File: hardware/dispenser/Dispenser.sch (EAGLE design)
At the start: 64 parts, among them J1 AVR_Prog, J2 RJ45-8PTH, Q1 NFET-SO8, Q2 NFET, Q3 NFET, Q4 NFET, Q5 MOSFET-NCHANNELSMD, U1 ATMEGA168, U10 HALL-EFFECT, U2 OPAMP-DUAL, U3 OPTO-TLP185, U4 MPX10DP, U5 VREG-5V-LDO-AP1117SOT89-3L, U6 WS2801, U7 HALL-EFFECT, U8 HALL-EFFECT, U9 HALL-EFFECT

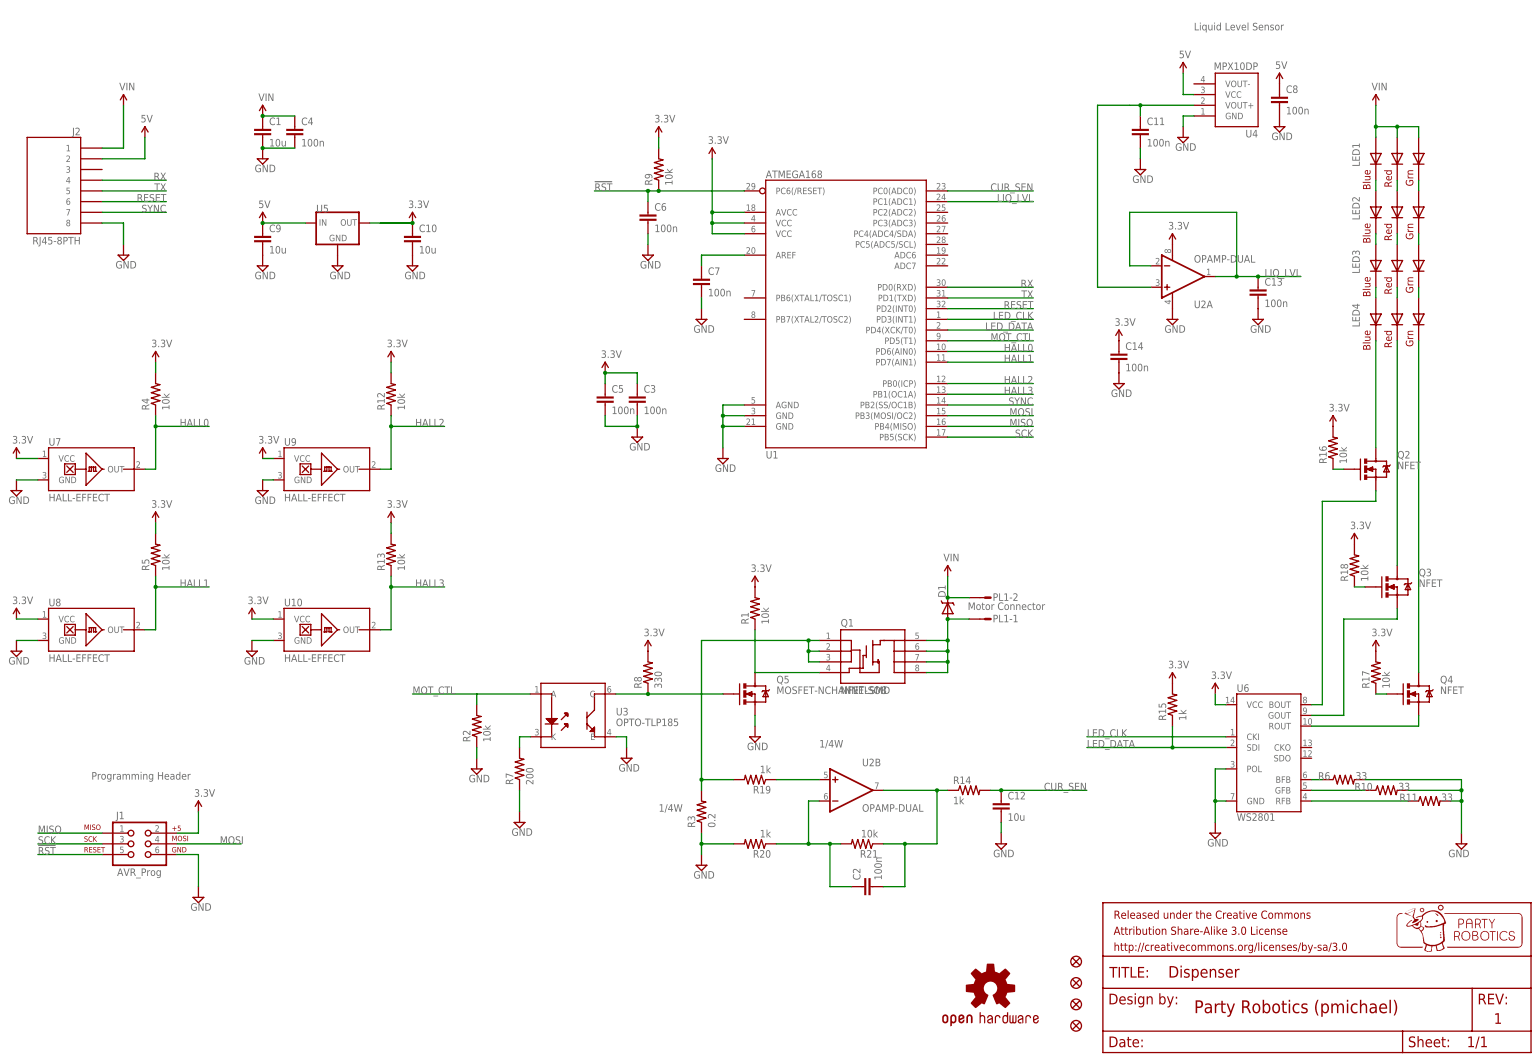
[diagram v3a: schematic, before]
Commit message: Current sense cap to 100u, and opto inputs changed again
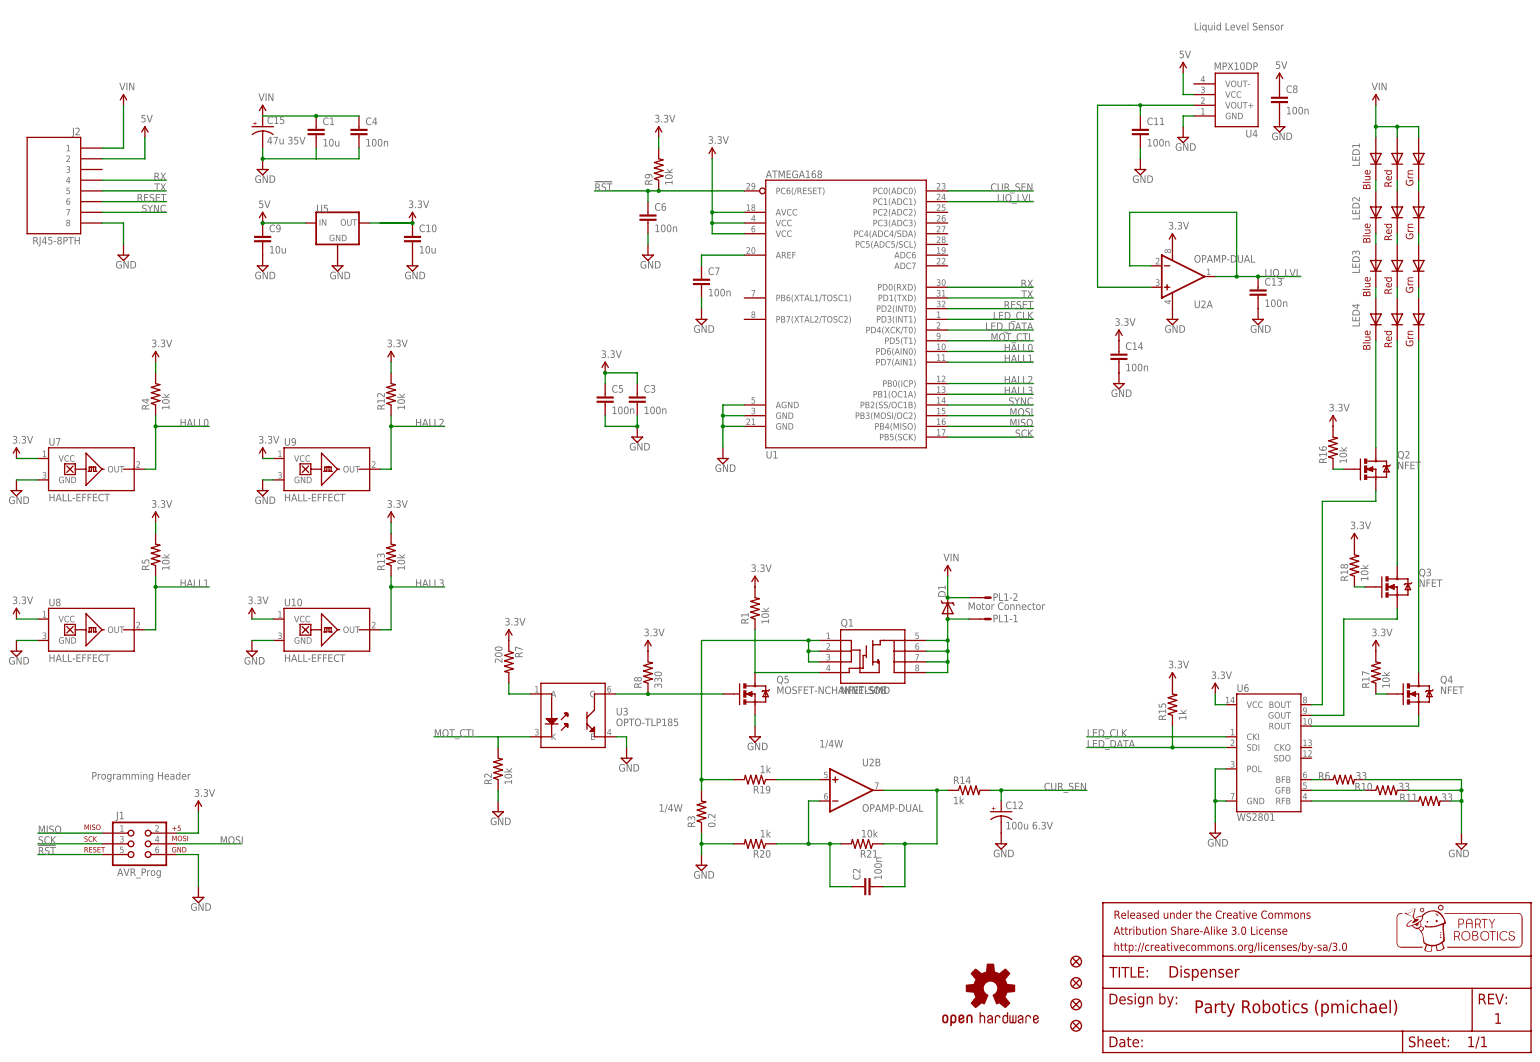
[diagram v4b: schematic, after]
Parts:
- added C15: 47u 35V, SparkFun-Capacitors:CAP_POLD
- C12: value 10u -> 100u 6.3V; device SparkFun-Capacitors:CAP1206 -> SparkFun-Capacitors:CAP_POLD
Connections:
- new net N$16: R7.2, U3.A
- net 3.3V: now also R7.1
- net CUR_SEN: now also C12.+; no longer C12.1
- net GND: now also C12.-; no longer C12.2, R7.1
- net MOT_CTL: now also U3.K; no longer U3.A
- net N$15: now also C15.-; no longer R7.2, U3.K
- net VIN: now also C15.+
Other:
- moved on the sheet: C1, C4, R2, R7
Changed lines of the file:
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@@
 <part name="R2" library="SparkFun-Resistors" deviceset="RESISTOR" device="0603-RES" value="10k"/>
 <part name="SUPPLY4" library="supply2" deviceset="GND" device=""/>
-<part name="C12" library="SparkFun-Capacitors" deviceset="CAP" device="1206" value="10u"/>
 <part name="SUPPLY5" library="supply2" deviceset="GND" device=""/>
 <part name="R14" library="SparkFun-Resistors" deviceset="RESISTOR" device="0603-RES" value="1k"/>
@@
 <part name="P+18" library="SparkFun-Aesthetics" deviceset="3.3V" device=""/>
 <part name="D1" library="pierre" deviceset="B330A" device=""/>
-<part name="SUPPLY22" library="supply2" deviceset="GND" device=""/>
+<part name="P+10" library="SparkFun-Aesthetics" deviceset="3.3V" device=""/>
+<part name="C12" library="SparkFun-Capacitors" deviceset="CAP_POL" device="D" value="100u 6.3V"/>
+<part name="C15" library="SparkFun-Capacitors" deviceset="CAP_POL" device="D" value="47u 35V"/>
 </parts>
 <sheets>
@@
 <instance part="C3" gate="G$1" x="172.72" y="157.48"/>
 <instance part="SUPPLY2" gate="GND" x="193.04" y="144.78"/>
-<instance part="C1" gate="G$1" x="83.82" y="220.98"/>
-<instance part="SUPPLY6" gate="GND" x="83.82" y="215.9"/>
+<instance part="C1" gate="G$1" x="96.52" y="220.98"/>
+<instance part="SUPPLY6" gate="GND" x="83.82" y="213.36"/>
 <instance part="U$13" gate="G$1" x="83.82" y="226.06"/>
 <instance part="Q1" gate="G$1" x="228.6" y="99.06"/>
 <instance part="U$14" gate="G$1" x="246.38" y="116.84"/>
 <instance part="U3" gate="G$1" x="157.48" y="83.82"/>
-<instance part="R7" gate="G$1" x="144.78" y="71.12" rot="R90"/>
+<instance part="R7" gate="G$1" x="142.24" y="96.52" rot="R270"/>
 <instance part="SUPPLY7" gate="GND" x="170.18" y="73.66"/>
 <instance part="R8" gate="G$1" x="175.26" y="93.98" rot="R90"/>
@@
 <instance part="GND" gate="GND" x="299.72" y="177.8"/>
 <instance part="U$3" gate="G$1" x="347.98" y="228.6"/>
-<instance part="C4" gate="G$1" x="91.44" y="220.98"/>
+<instance part="C4" gate="G$1" x="106.68" y="220.98"/>
 <instance part="R6" gate="G$1" x="340.36" y="68.58" smashed="yes">
 <attribute name="NAME" x="334.264" y="68.5546" size="1.778" layer="95"/>
@@
 <attribute name="VALUE" x="363.474" y="63.5" size="1.778" layer="96"/>
 </instance>
-<instance part="R2" gate="G$1" x="134.62" y="81.28" rot="R90"/>
-<instance part="SUPPLY4" gate="GND" x="134.62" y="71.12"/>
-<instance part="C12" gate="G$1" x="259.08" y="60.96"/>
+<instance part="R2" gate="G$1" x="139.7" y="71.12" rot="R90"/>
+<instance part="SUPPLY4" gate="GND" x="139.7" y="60.96"/>
 <instance part="SUPPLY5" gate="GND" x="259.08" y="53.34"/>
 <instance part="R14" gate="G$1" x="251.46" y="66.04"/>
@@
 <instance part="P+18" gate="G$1" x="200.66" y="114.3"/>
 <instance part="D1" gate="G$1" x="246.38" y="109.22" rot="R90"/>
-<instance part="SUPPLY22" gate="GND" x="144.78" y="58.42"/>
+<instance part="P+10" gate="G$1" x="142.24" y="101.6"/>
+<instance part="C12" gate="G$1" x="259.08" y="60.96"/>
+<instance part="C15" gate="G$1" x="83.82" y="223.52"/>
 </instances>
 <busses>
@@
 <pinref part="SUPPLY6" gate="GND" pin="GND"/>
 <pinref part="C4" gate="G$1" pin="2"/>
-<wire x1="91.44" y1="218.44" x2="83.82" y2="218.44" width="0.1524" layer="91"/>
-<junction x="83.82" y="218.44"/>
+<wire x1="106.68" y1="218.44" x2="106.68" y2="215.9" width="0.1524" layer="91"/>
+<wire x1="106.68" y1="215.9" x2="96.52" y2="215.9" width="0.1524" layer="91"/>
+<junction x="83.82" y="215.9"/>
+<wire x1="83.82" y1="215.9" x2="96.52" y2="215.9" width="0.1524" layer="91"/>
+<wire x1="96.52" y1="215.9" x2="96.52" y2="218.44" width="0.1524" layer="91"/>
 </segment>
 <segment>
@@
 <pinref part="R2" gate="G$1" pin="1"/>
 <pinref part="SUPPLY4" gate="GND" pin="GND"/>
-<wire x1="134.62" y1="76.2" x2="134.62" y2="73.66" width="0.1524" layer="91"/>
+<wire x1="139.7" y1="66.04" x2="139.7" y2="63.5" width="0.1524" layer="91"/>
 </segment>
 <segment>
-<pinref part="C12" gate="G$1" pin="2"/>
 <pinref part="SUPPLY5" gate="GND" pin="GND"/>
-<wire x1="259.08" y1="58.42" x2="259.08" y2="55.88" width="0.1524" layer="91"/>
+<pinref part="C12" gate="G$1" pin="-"/>
 </segment>
 <segment>
@@
 <wire x1="200.66" y1="81.28" x2="200.66" y2="83.82" width="0.1524" layer="91"/>
 </segment>
-<segment>
-<pinref part="R7" gate="G$1" pin="1"/>
-<wire x1="144.78" y1="66.04" x2="144.78" y2="60.96" width="0.1524" layer="91"/>
-<pinref part="SUPPLY22" gate="GND" pin="GND"/>
-</segment>
 </net>
 <net name="5V" class="0">
@@
 <pinref part="P+18" gate="G$1" pin="3.3V"/>
 </segment>
+<segment>
+<pinref part="R7" gate="G$1" pin="1"/>
+<pinref part="P+10" gate="G$1" pin="3.3V"/>
+</segment>
 </net>
 <net name="LED_CLK" class="0">
@@
 </segment>
 <segment>
-<pinref part="C12" gate="G$1" pin="1"/>
-<wire x1="259.08" y1="66.04" x2="279.4" y2="66.04" width="0.1524" layer="91"/>
-<junction x="259.08" y="66.04"/>
 <wire x1="256.54" y1="66.04" x2="259.08" y2="66.04" width="0.1524" layer="91"/>
 <label x="279.4" y="66.04" size="1.778" layer="95" rot="MR0"/>
 <pinref part="R14" gate="G$1" pin="2"/>
+<pinref part="C12" gate="G$1" pin="+"/>
+<wire x1="259.08" y1="63.5" x2="259.08" y2="66.04" width="0.1524" layer="91"/>
+<wire x1="259.08" y1="66.04" x2="279.4" y2="66.04" width="0.1524" layer="91"/>
+<junction x="259.08" y="66.04"/>
 </segment>
 </net>
@@
 <pinref part="U$13" gate="G$1" pin="VIN"/>
 <pinref part="C4" gate="G$1" pin="1"/>
-<wire x1="91.44" y1="226.06" x2="83.82" y2="226.06" width="0.1524" layer="91"/>
-<junction x="83.82" y="226.06"/>
+<wire x1="106.68" y1="226.06" x2="96.52" y2="226.06" width="0.1524" layer="91"/>
+<junction x="96.52" y="226.06"/>
+<pinref part="C15" gate="G$1" pin="+"/>
+<wire x1="96.52" y1="226.06" x2="83.82" y2="226.06" width="0.1524" layer="91"/>
 </segment>
 <segment>
@@
 <net name="MOT_CTL" class="0">
 <segment>
-<label x="119.38" y="88.9" size="1.778" layer="95"/>
-<wire x1="134.62" y1="86.36" x2="134.62" y2="88.9" width="0.2032" layer="91"/>
-<wire x1="134.62" y1="88.9" x2="119.38" y2="88.9" width="0.2032" layer="91"/>
+<label x="124.46" y="78.74" size="1.778" layer="95"/>
+<wire x1="139.7" y1="76.2" x2="139.7" y2="78.74" width="0.2032" layer="91"/>
+<wire x1="139.7" y1="78.74" x2="124.46" y2="78.74" width="0.2032" layer="91"/>
 <pinref part="R2" gate="G$1" pin="2"/>
-<pinref part="U3" gate="G$1" pin="A"/>
-<wire x1="134.62" y1="88.9" x2="147.32" y2="88.9" width="0.1524" layer="91"/>
+<pinref part="U3" gate="G$1" pin="K"/>
+<wire x1="147.32" y1="78.74" x2="139.7" y2="78.74" width="0.1524" layer="91"/>
 </segment>
 <segment>
@@
 </segment>
 </net>
-<net name="N$15" class="0">
+<net name="N$16" class="0">
 <segment>
 <pinref part="R7" gate="G$1" pin="2"/>
-<wire x1="144.78" y1="76.2" x2="144.78" y2="78.74" width="0.1524" layer="91"/>
-<pinref part="U3" gate="G$1" pin="K"/>
-<wire x1="144.78" y1="78.74" x2="147.32" y2="78.74" width="0.1524" layer="91"/>
+<wire x1="142.24" y1="91.44" x2="142.24" y2="88.9" width="0.1524" layer="91"/>
+<pinref part="U3" gate="G$1" pin="A"/>
+<wire x1="142.24" y1="88.9" x2="147.32" y2="88.9" width="0.1524" layer="91"/>
+</segment>
+</net>
+<net name="N$15" class="0">
+<segment>
+<pinref part="C15" gate="G$1" pin="-"/>
+<wire x1="83.82" y1="218.44" x2="83.82" y2="215.9" width="0.1524" layer="91"/>
 </segment>
 </net>

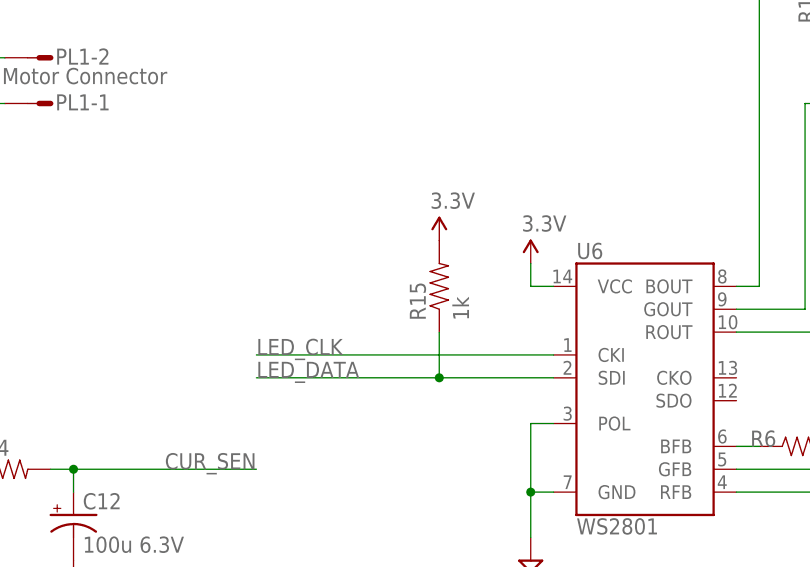
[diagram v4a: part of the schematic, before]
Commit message: removed LED_DATA pull up
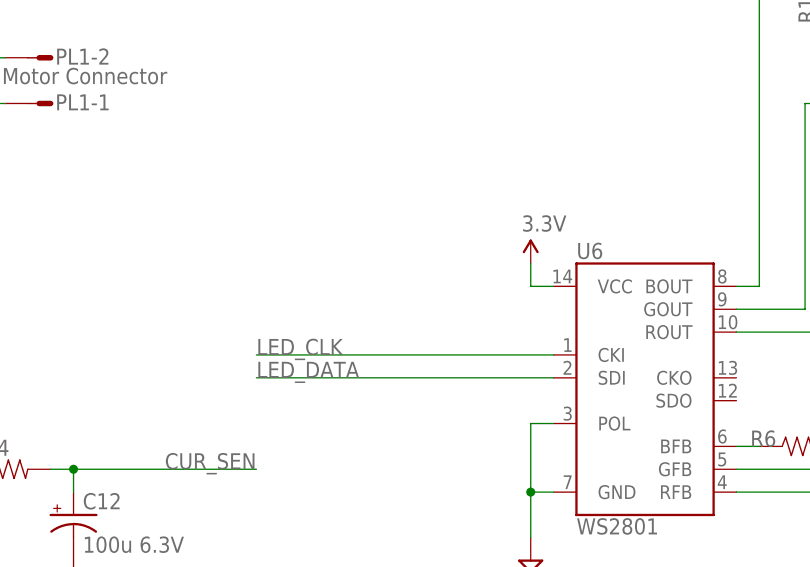
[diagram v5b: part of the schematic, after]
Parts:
- removed R15: 1k, SparkFun-Resistors:RESISTOR0603-RES
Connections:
- net 3.3V: no longer R15.2
- net LED_DATA: no longer R15.1
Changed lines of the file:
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@@
 <part name="SUPPLY23" library="supply2" deviceset="GND" device=""/>
 <part name="SUPPLY24" library="supply2" deviceset="GND" device=""/>
-<part name="R15" library="SparkFun-Resistors" deviceset="RESISTOR" device="0603-RES" value="1k"/>
-<part name="P+21" library="SparkFun-Aesthetics" deviceset="3.3V" device=""/>
 <part name="C11" library="SparkFun" deviceset="CAP" device="0603-CAP" value="100n"/>
 <part name="SUPPLY25" library="supply2" deviceset="GND" device=""/>
@@
 <instance part="SUPPLY23" gate="GND" x="309.88" y="55.88"/>
 <instance part="SUPPLY24" gate="GND" x="368.3" y="53.34" rot="MR0"/>
-<instance part="R15" gate="G$1" x="299.72" y="86.36" rot="R90"/>
-<instance part="P+21" gate="G$1" x="299.72" y="91.44"/>
 <instance part="C11" gate="G$1" x="292.1" y="220.98"/>
 <instance part="SUPPLY25" gate="GND" x="292.1" y="213.36"/>
@@
 </segment>
 <segment>
-<pinref part="R15" gate="G$1" pin="2"/>
-<pinref part="P+21" gate="G$1" pin="3.3V"/>
-</segment>
-<segment>
 <pinref part="R17" gate="G$1" pin="2"/>
 <pinref part="P+24" gate="G$1" pin="3.3V"/>
@@
 <segment>
 <pinref part="U6" gate="G$1" pin="SDI"/>
-<wire x1="312.42" y1="76.2" x2="299.72" y2="76.2" width="0.1524" layer="91"/>
 <label x="279.4" y="76.2" size="1.778" layer="95"/>
-<pinref part="R15" gate="G$1" pin="1"/>
-<wire x1="299.72" y1="76.2" x2="279.4" y2="76.2" width="0.1524" layer="91"/>
-<wire x1="299.72" y1="81.28" x2="299.72" y2="76.2" width="0.1524" layer="91"/>
-<junction x="299.72" y="76.2"/>
+<wire x1="312.42" y1="76.2" x2="279.4" y2="76.2" width="0.1524" layer="91"/>
 </segment>
 </net>
